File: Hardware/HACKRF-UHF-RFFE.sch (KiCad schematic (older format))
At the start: 2 parts, among them J1 SMA_Wurth_60312242114510, J2 SMA_Wurth_60312242114510

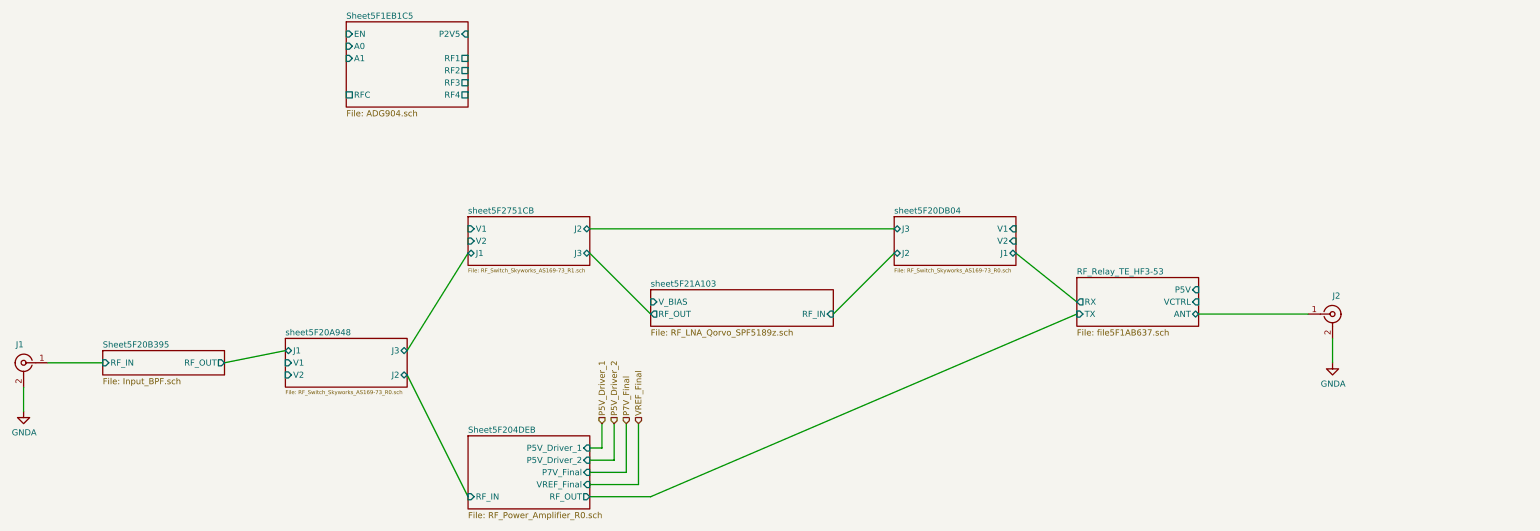
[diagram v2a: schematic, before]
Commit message: Improving LNA simulations and Documentation package. More to come on this one.
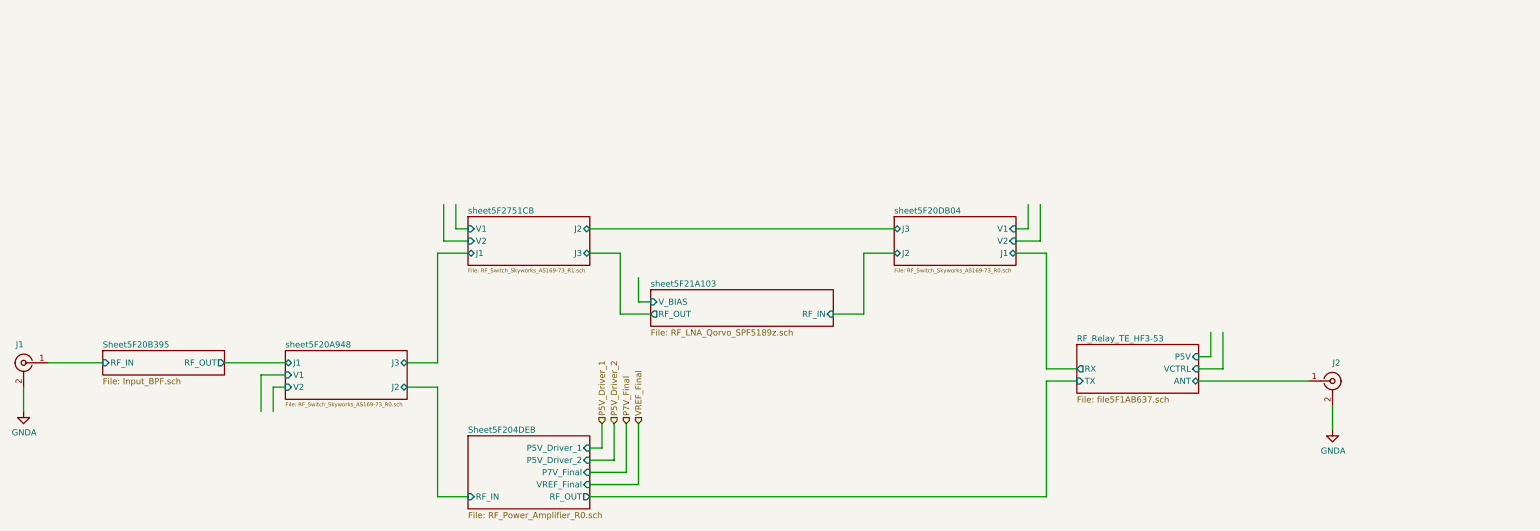
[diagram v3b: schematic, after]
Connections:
- wire segments 21 -> 50
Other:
- moved on the sheet: J2
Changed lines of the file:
@@
 $Descr User 17000 11000
 encoding utf-8
-Sheet 1 24
+Sheet 1 23
 Title "HackRF One Frontend"
 Date "2020-07-04"
@@
 	3050 4800 3500 4800
 $Sheet
-S 11500 4100 1000 400
+S 11500 4650 1000 400
 U 5F1AB638
 F0 "RF_Relay_TE_HF3-53" 50
 F1 "file5F1AB637.sch" 50
-F2 "VCTRL" I R 12500 4300 50
-F3 "RX" O L 11500 4300 50
-F4 "TX" I L 11500 4400 50
-F5 "ANT" B R 12500 4400 50
-F6 "P5V" I R 12500 4200 50
-$EndSheet
-Wire Wire Line
-	13400 4400 12500 4400
-$Sheet
-S 5000 4600 1000 400
+F2 "VCTRL" I R 12500 4850 50
+F3 "RX" O L 11500 4850 50
+F4 "TX" I L 11500 4950 50
+F5 "ANT" B R 12500 4950 50
+F6 "P5V" I R 12500 4750 50
+$EndSheet
+Wire Wire Line
+	13400 4950 12500 4950
+$Sheet
+S 5000 4700 1000 400
 U 5F20A94F
 F0 "sheet5F20A948" 50
 F1 "RF_Switch_Skyworks_AS169-73_R0.sch" 32
-F2 "J1" B L 5000 4700 50
-F3 "J3" B R 6000 4700 50
-F4 "J2" B R 6000 4900 50
-F5 "V1" I L 5000 4800 50
-F6 "V2" I L 5000 4900 50
+F2 "J1" B L 5000 4800 50
+F3 "J3" B R 6000 4800 50
+F4 "J2" B R 6000 5000 50
+F5 "V1" I L 5000 4900 50
+F6 "V2" I L 5000 5000 50
 $EndSheet
 Wire Wire Line
@@
 $EndSheet
 Wire Wire Line
-	9500 4400 10000 3900
-Wire Wire Line
-	11000 3900 11500 4300
-Wire Wire Line
-	13600 4600 13600 4800
+	13600 5150 13600 5350
 $Sheet
 S 10000 3600 1000 400
@@
 L power:GNDA #PWR02
 U 1 1 5F25C5EB
-P 13600 4800
-F 0 "#PWR02" H 13600 4550 50  0001 C CNN
-F 1 "GNDA" H 13605 4627 50  0000 C CNN
-F 2 "" H 13600 4800 50  0001 C CNN
-F 3 "" H 13600 4800 50  0001 C CNN
-	1    13600 4800
+P 13600 5350
+F 0 "#PWR02" H 13600 5100 50  0001 C CNN
+F 1 "GNDA" H 13605 5177 50  0000 C CNN
+F 2 "" H 13600 5350 50  0001 C CNN
+F 3 "" H 13600 5350 50  0001 C CNN
+	1    13600 5350
 	1    0    0    -1
 $EndComp
@@
 L RF:SMA_Wurth_60312242114510 J2
 U 1 1 5F1A3F2A
-P 13600 4400
-F 0 "J2" H 13600 4550 50  0000 L CNN
-F 1 "SMA_Wurth_60312242114510" H 13528 4547 50  0001 C CNN
-F 2 "RF:SMA_Wurth_60312242114510" H 13600 4400 50  0001 C CNN
-F 3 "https://www.we-online.de/katalog/datasheet/60312242114510.pdf" H 13600 4400 50  0001 C CNN
-	1    13600 4400
+P 13600 4950
+F 0 "J2" H 13600 5100 50  0000 L CNN
+F 1 "SMA_Wurth_60312242114510" H 13528 5097 50  0001 C CNN
+F 2 "RF:SMA_Wurth_60312242114510" H 13600 4950 50  0001 C CNN
+F 3 "https://www.we-online.de/katalog/datasheet/60312242114510.pdf" H 13600 4950 50  0001 C CNN
+	1    13600 4950
 	1    0    0    -1
 $EndComp
@@
 F3 "RF_OUT" O R 4500 4800 50
 $EndSheet
-Wire Wire Line
-	4500 4800 5000 4700
 $Sheet
 S 6500 5400 1000 600
@@
 $EndSheet
 Wire Wire Line
-	6000 4900 6500 5900
-Wire Wire Line
-	6000 4700 6500 3900
-Wire Wire Line
-	7500 3900 8000 4400
-Wire Wire Line
 	7500 3700 10000 3700
 Wire Wire Line
@@
 	7500 5800 7900 5800
 Wire Wire Line
-	7500 5900 8000 5900
-Wire Wire Line
-	11500 4400 8000 5900
-$Sheet
-S 5500 2000 1000 700
-U 5F1EB1C6
-F0 "Sheet5F1EB1C5" 50
-F1 "ADG904.sch" 50
-F2 "P2V5" I R 6500 2100 50
-F3 "RF1" U R 6500 2300 50
-F4 "RF2" U R 6500 2400 50
-F5 "RF3" U R 6500 2500 50
-F6 "RF4" U R 6500 2600 50
-F7 "RFC" U L 5500 2600 50
-F8 "EN" I L 5500 2100 50
-F9 "A0" I L 5500 2200 50
-F10 "A1" I L 5500 2300 50
-$EndSheet
+	6000 4800 6250 4800
+Wire Wire Line
+	6250 3900 6500 3900
+Wire Wire Line
+	6000 5000 6250 5000
+Wire Wire Line
+	6250 5900 6500 5900
+Wire Wire Line
+	11250 5900 11250 4950
+Wire Wire Line
+	11250 4950 11500 4950
+Wire Wire Line
+	7500 5900 11250 5900
+Wire Wire Line
+	7500 3900 7750 3900
+Wire Wire Line
+	7750 3900 7750 4400
+Wire Wire Line
+	7750 4400 8000 4400
+Wire Wire Line
+	9500 4400 9750 4400
+Wire Wire Line
+	9750 4400 9750 3900
+Wire Wire Line
+	9750 3900 10000 3900
+Wire Wire Line
+	11000 3900 11250 3900
+Wire Wire Line
+	11250 4850 11500 4850
+Wire Wire Line
+	5000 5000 4900 5000
+Wire Wire Line
+	4900 5000 4900 5200
+Wire Wire Line
+	5000 4900 4800 4900
+Wire Wire Line
+	4800 4900 4800 5200
+Wire Wire Line
+	6500 3700 6400 3700
+Wire Wire Line
+	6400 3700 6400 3500
+Wire Wire Line
+	6500 3800 6300 3800
+Wire Wire Line
+	6300 3800 6300 3500
+Wire Wire Line
+	11000 3700 11100 3700
+Wire Wire Line
+	11100 3700 11100 3500
+Wire Wire Line
+	11000 3800 11200 3800
+Wire Wire Line
+	11200 3800 11200 3500
+Wire Wire Line
+	12500 4750 12600 4750
+Wire Wire Line
+	12600 4750 12600 4550
+Wire Wire Line
+	12500 4850 12700 4850
+Wire Wire Line
+	12700 4850 12700 4550
+Wire Wire Line
+	8000 4300 7900 4300
+Wire Wire Line
+	7900 4300 7900 4100
+Wire Wire Line
+	6250 5000 6250 5900
+Wire Wire Line
+	4500 4800 5000 4800
+Wire Wire Line
+	6250 3900 6250 4800
+Wire Wire Line
+	11250 3900 11250 4850
 $EndSCHEMATC
